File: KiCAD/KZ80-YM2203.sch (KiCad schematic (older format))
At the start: 32 parts, among them J1 SBC8080 BUS, J2 AD-JP1, J3 AD-JP1, J4 OUTPUT, U1 LM358, U2 74LS139, U3 74HCU04, U4 YM2203, U5 YM3014B, Y1 3.8MHz

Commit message: パス見直し
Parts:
- J1: symbol Z80-CPUB-rescue:Conn_02x20_Odd_Even -> KZ80-YM2203-rescue:Conn_02x20_Odd_Even-Z80-CPUB-rescue
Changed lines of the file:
@@
 EESchema Schematic File Version 4
+LIBS:KZ80-YM2203-cache
 EELAYER 30 0
 EELAYER END
@@
 	8300 1950 8350 1950
 $Comp
-L Z80-CPUB-rescue:Conn_02x20_Odd_Even J1
+L KZ80-YM2203-rescue:Conn_02x20_Odd_Even-Z80-CPUB-rescue J1
 U 1 1 5B55D8C4
 P 1150 1850
@@
 Wire Wire Line
 	2450 4600 2450 4700
+Connection ~ 2450 4600
+Wire Wire Line
+	2450 4600 2600 4600
 Wire Bus Line
 	1900 550  1900 3400
@@
 Wire Bus Line
 	600  550  600  4150
-Connection ~ 2450 4600
-Wire Wire Line
-	2450 4600 2600 4600
 $EndSCHEMATC

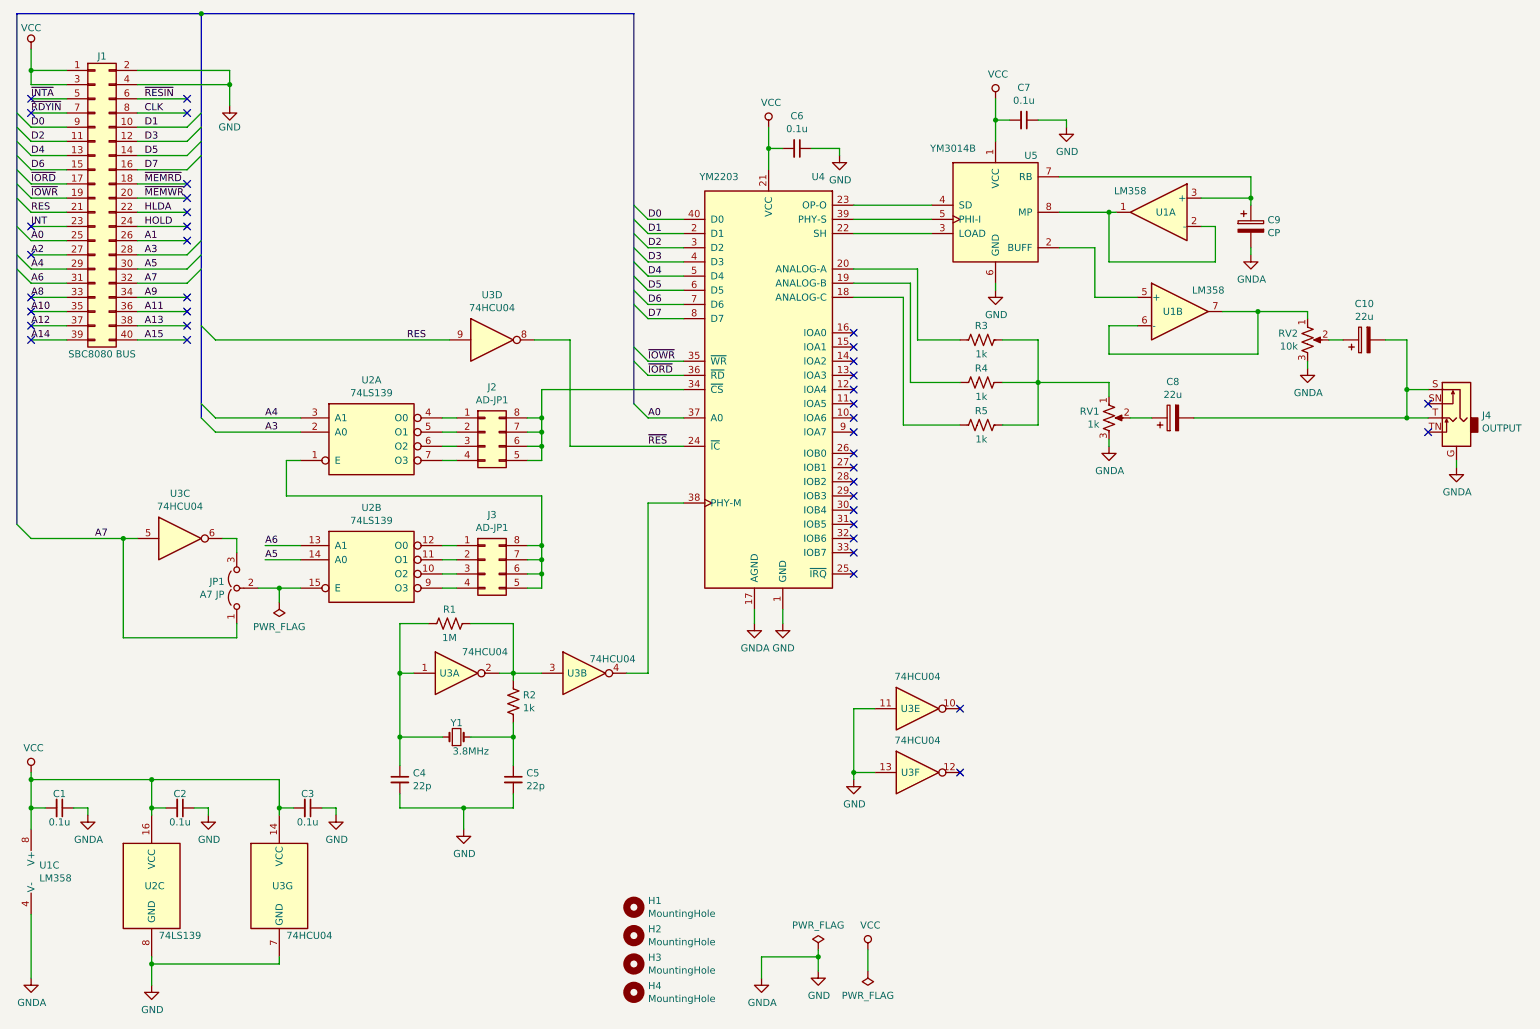
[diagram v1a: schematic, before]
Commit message: 回路図 間違いなど修正。出力段に抵抗器装着
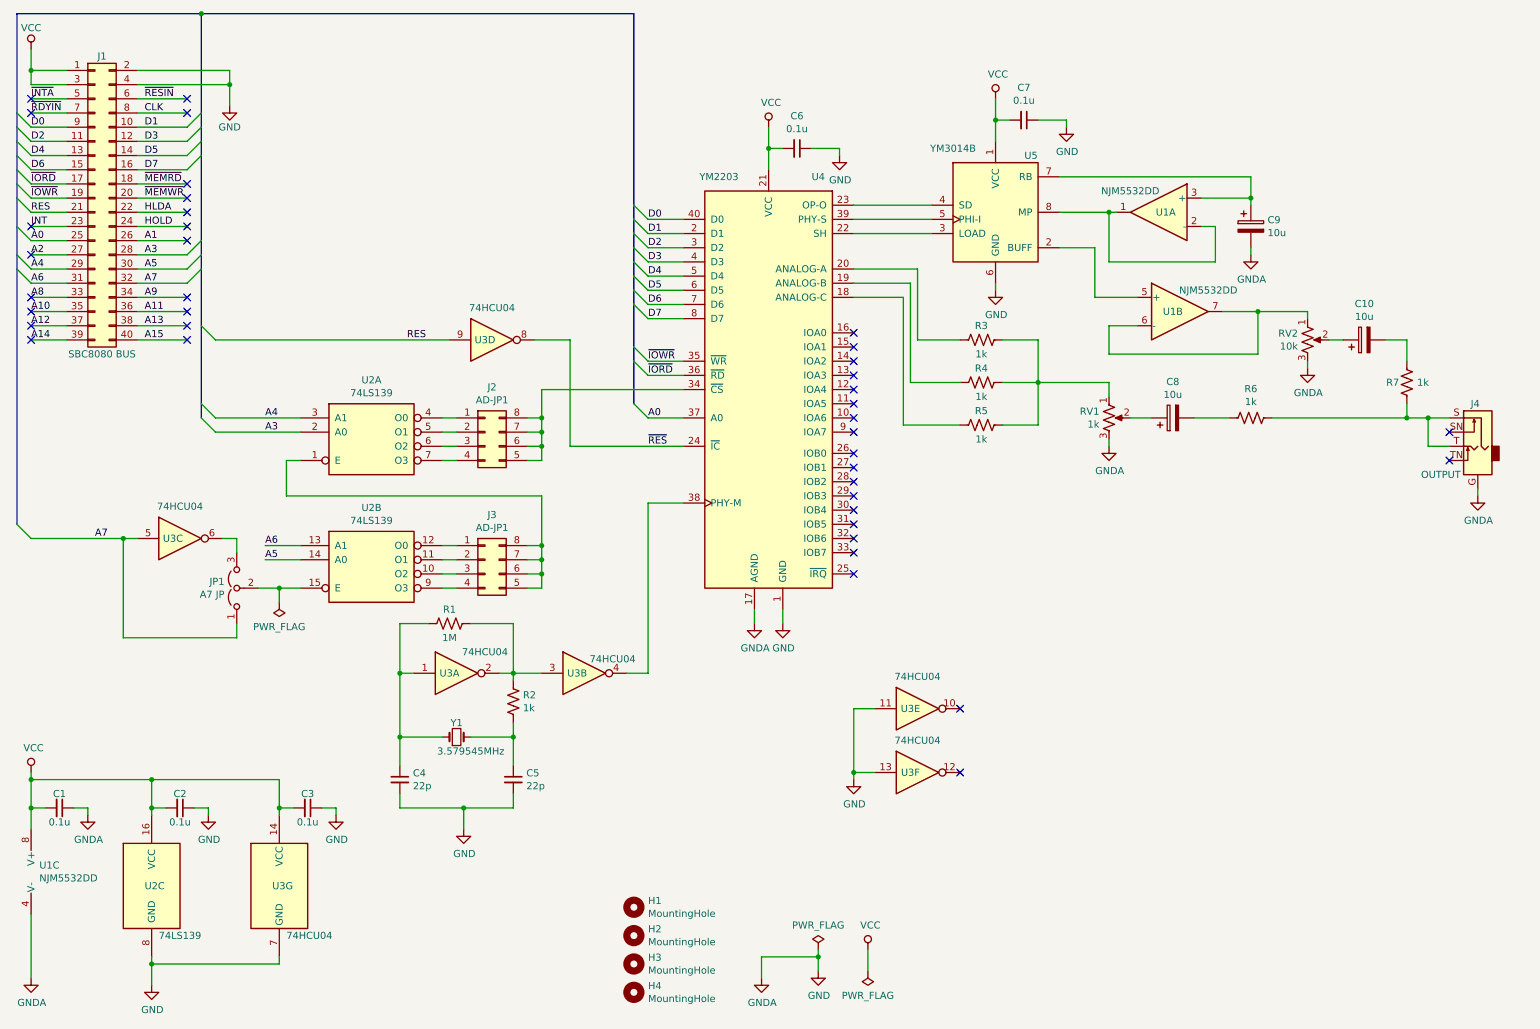
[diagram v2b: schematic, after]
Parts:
- added R6, R7: 1k, symbol Device:R_US
- C10, C8: value 22u -> 10u
- C9: value CP -> 10u
- U1: value LM358 -> NJM5532DD
- Y1: value 3.8MHz -> 3.579545MHz
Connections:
- net at J4.S, J4.T: now also R6.1, R7.1; no longer C10.2, C8.2
- new net: C8.2, R6.2
- new net: C10.2, R7.2
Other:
- moved on the sheet: J4
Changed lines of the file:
@@
 EESchema Schematic File Version 4
-LIBS:KZ80-YM2203-cache
 EELAYER 30 0
 EELAYER END
@@
 P 8650 1950
 F 0 "U1" H 8600 1950 50  0000 C CNN
-F 1 "LM358" H 8850 2100 50  0000 C CNN
+F 1 "NJM5532DD" H 8850 2100 50  0000 C CNN
 F 2 "" H 8650 1950 50  0001 C CNN
-F 3 "http://www.ti.com/lit/ds/symlink/lm2904-n.pdf" H 8650 1950 50  0001 C CNN
+F 3 "https://www.njr.co.jp/products/semicon/PDF/NJM5532_J.pdf" H 8650 1950 50  0001 C CNN
 	1    8650 1950
 	-1   0    0    -1
@@
 P 8800 2650
 F 0 "U1" H 8750 2650 50  0000 C CNN
-F 1 "LM358" H 9000 2800 50  0000 C CNN
+F 1 "NJM5532DD" H 9000 2800 50  0000 C CNN
 F 2 "" H 8800 2650 50  0001 C CNN
-F 3 "http://www.ti.com/lit/ds/symlink/lm2904-n.pdf" H 8800 2650 50  0001 C CNN
+F 3 "https://www.njr.co.jp/products/semicon/PDF/NJM5532_J.pdf" H 8800 2650 50  0001 C CNN
 	2    8800 2650
 	1    0    0    -1
@@
 P 800 6600
 F 0 "U1" H 758 6646 50  0000 L CNN
-F 1 "LM358" H 758 6555 50  0000 L CNN
+F 1 "NJM5532DD" H 758 6555 50  0000 L CNN
 F 2 "" H 800 6600 50  0001 C CNN
-F 3 "http://www.ti.com/lit/ds/symlink/lm2904-n.pdf" H 800 6600 50  0001 C CNN
+F 3 "https://www.njr.co.jp/products/semicon/PDF/NJM5532_J.pdf" H 800 6600 50  0001 C CNN
 	3    800  6600
 	1    0    0    -1
@@
 U 3 1 5FBD20EB
 P 1750 4250
-F 0 "U3" H 1750 4567 50  0000 C CNN
+F 0 "U3" H 1700 4250 50  0000 C CNN
 F 1 "74HCU04" H 1750 4476 50  0000 C CNN
 F 2 "" H 1750 4250 50  0001 C CNN
@@
 U 4 1 5FBD28D0
 P 3950 2850
-F 0 "U3" H 3950 3167 50  0000 C CNN
+F 0 "U3" H 3900 2850 50  0000 C CNN
 F 1 "74HCU04" H 3950 3076 50  0000 C CNN
 F 2 "" H 3950 2850 50  0001 C CNN
@@
 P 3700 5650
 F 0 "Y1" H 3700 5750 50  0000 C CNN
-F 1 "3.8MHz" H 3800 5550 50  0000 C CNN
+F 1 "3.579545MHz" H 3800 5550 50  0000 C CNN
 F 2 "" H 3700 5650 50  0001 C CNN
 F 3 "~" H 3700 5650 50  0001 C CNN
@@
 P 8750 3400
 F 0 "C8" V 9005 3400 50  0000 C CNN
-F 1 "22u" V 8914 3400 50  0000 C CNN
+F 1 "10u" V 8914 3400 50  0000 C CNN
 F 2 "" H 8788 3250 50  0001 C CNN
 F 3 "~" H 8750 3400 50  0001 C CNN
@@
 P 10100 2850
 F 0 "C10" V 10355 2850 50  0000 C CNN
-F 1 "22u" V 10264 2850 50  0000 C CNN
+F 1 "10u" V 10264 2850 50  0000 C CNN
 F 2 "" H 10138 2700 50  0001 C CNN
 F 3 "~" H 10100 2850 50  0001 C CNN
@@
 Wire Wire Line
 	8450 3400 8600 3400
-Wire Wire Line
-	8900 3400 10400 3400
-Wire Wire Line
-	10400 3400 10400 3200
 Wire Wire Line
 	10400 2850 10250 2850
@@
 L Connector:AudioJack2_Ground_Switch J4
 U 1 1 60090806
-P 10750 3400
-F 0 "J4" H 10570 3418 50  0000 R CNN
-F 1 "OUTPUT" H 10570 3327 50  0000 R CNN
-F 2 "" H 10750 3600 50  0001 C CNN
-F 3 "~" H 10750 3600 50  0001 C CNN
-	1    10750 3400
+P 10900 3600
+F 0 "J4" H 10950 3900 50  0000 R CNN
+F 1 "OUTPUT" H 11300 3400 50  0000 R CNN
+F 2 "" H 10900 3800 50  0001 C CNN
+F 3 "~" H 10900 3800 50  0001 C CNN
+	1    10900 3600
 	-1   0    0    -1
 $EndComp
-Wire Wire Line
-	10400 3400 10550 3400
-Connection ~ 10400 3400
-Wire Wire Line
-	10400 3200 10550 3200
-Connection ~ 10400 3200
-Wire Wire Line
-	10400 3200 10400 2850
-NoConn ~ 10550 3300
-NoConn ~ 10550 3500
-$Comp
-L power:GNDA #PWR024
-U 1 1 600D75A0
-P 10750 3750
-F 0 "#PWR024" H 10750 3500 50  0001 C CNN
-F 1 "GNDA" H 10755 3577 50  0000 C CNN
-F 2 "" H 10750 3750 50  0001 C CNN
-F 3 "" H 10750 3750 50  0001 C CNN
-	1    10750 3750
-	1    0    0    -1
-$EndComp
-Wire Wire Line
-	10750 3700 10750 3750
+NoConn ~ 10700 3500
+NoConn ~ 10700 3700
 $Comp
 L Device:CP C9
@@
 P 9300 2050
 F 0 "C9" H 9418 2096 50  0000 L CNN
-F 1 "CP" H 9418 2005 50  0000 L CNN
+F 1 "10u" H 9418 2005 50  0000 L CNN
 F 2 "" H 9338 1900 50  0001 C CNN
 F 3 "~" H 9300 2050 50  0001 C CNN
@@
 Wire Wire Line
 	2450 4600 2600 4600
-Wire Bus Line
-	1900 550  1900 3400
+Wire Wire Line
+	10900 3900 10900 3950
+$Comp
+L power:GNDA #PWR024
+U 1 1 600D75A0
+P 10900 3950
+F 0 "#PWR024" H 10900 3700 50  0001 C CNN
+F 1 "GNDA" H 10905 3777 50  0000 C CNN
+F 2 "" H 10900 3950 50  0001 C CNN
+F 3 "" H 10900 3950 50  0001 C CNN
+	1    10900 3950
+	1    0    0    -1
+$EndComp
+$Comp
+L Device:R_US R6
+U 1 1 5FCD251E
+P 9300 3400
+F 0 "R6" V 9095 3400 50  0000 C CNN
+F 1 "1k" V 9186 3400 50  0000 C CNN
+F 2 "" V 9340 3390 50  0001 C CNN
+F 3 "~" H 9300 3400 50  0001 C CNN
+	1    9300 3400
+	0    1    1    0
+$EndComp
+$Comp
+L Device:R_US R7
+U 1 1 5FD00CC1
+P 10400 3150
+F 0 "R7" H 10500 3150 50  0000 C CNN
+F 1 "1k" H 10286 3150 50  0000 C CNN
+F 2 "" V 10440 3140 50  0001 C CNN
+F 3 "~" H 10400 3150 50  0001 C CNN
+	1    10400 3150
+	-1   0    0    1
+$EndComp
+Wire Wire Line
+	10400 2850 10400 3000
+Wire Wire Line
+	8900 3400 9150 3400
+Wire Wire Line
+	9450 3400 10400 3400
+Wire Wire Line
+	10400 3300 10400 3400
+Connection ~ 10400 3400
+Wire Wire Line
+	10400 3400 10550 3400
+Wire Wire Line
+	10550 3400 10550 3600
+Wire Wire Line
+	10550 3600 10700 3600
 Wire Bus Line
 	4950 550  4950 3300
 Wire Bus Line
 	600  550  600  4150
+Wire Bus Line
+	1900 550  1900 3400
+Connection ~ 10550 3400
+Wire Wire Line
+	10550 3400 10700 3400
 $EndSCHEMATC

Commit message: 基板パターン検討・ガーバーデータ出力
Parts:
- removed J4: OUTPUT, symbol Connector:AudioJack2_Ground_Switch
- added C11: 10u, Capacitor_THT:CP_Radial_D5.0mm_P2.50mm, symbol Device:CP
- added J4: Audio-Jack, AJ-1780:AJ-1780, symbol AJ-1780:Audio-Jack-3_2Switches-YM2151-rescue
- added J5: A-CON, Connector_PinHeader_2.54mm:PinHeader_2x07_P2.54mm_Vertical, symbol Connector_Generic:Conn_02x07_Odd_Even
- added J6: B-CON, Connector_PinHeader_2.54mm:PinHeader_2x07_P2.54mm_Vertical, symbol Connector_Generic:Conn_02x07_Odd_Even
- added NT1: Net-Tie_2, NetTie:NetTie-2_SMD_Pad2.0mm, symbol Device:Net-Tie_2
- C1, C2, C3, C4, C5, C6, C7: footprint (none) -> Capacitor_THT:C_Disc_D3.0mm_W1.6mm_P2.50mm
- C10, C8, C9: footprint (none) -> Capacitor_THT:CP_Radial_D5.0mm_P2.50mm
- H1, H2, H3, H4: footprint (none) -> MountingHole:MountingHole_3.2mm_M3
- J2, J3: footprint (none) -> Connector_PinHeader_2.54mm:PinHeader_2x04_P2.54mm_Vertical; symbol Connector_Generic:Conn_02x04_Counter_Clockwise -> Connector_Generic:Conn_02x04_Odd_Even
- JP1: footprint (none) -> Connector_PinHeader_2.54mm:PinHeader_1x03_P2.54mm_Vertical
- R1, R2, R3, R4, R5, R6, R7: footprint (none) -> Resistor_THT:R_Axial_DIN0207_L6.3mm_D2.5mm_P10.16mm_Horizontal
- RV1, RV2: footprint (none) -> Potentiometer_THT:Potentiometer_Vishay_T73YP_Vertical
- U1: footprint (none) -> Package_DIP:DIP-8_W7.62mm_Socket
- U2: value 74LS139 -> 74HC139; footprint (none) -> Package_DIP:DIP-16_W7.62mm_Socket
- U3: footprint (none) -> Package_DIP:DIP-14_W7.62mm_Socket
- U4: footprint (none) -> Package_DIP:DIP-40_W15.24mm_Socket
- U5: footprint (none) -> Package_DIP:DIP-8_W7.62mm
- Y1: footprint (none) -> Crystal:Crystal_HC49-U_Vertical
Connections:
- net GND: now also C11.1, J5.14 (Pin_14), J6.14 (Pin_14), NT1.2; no longer C1.1, C7.1, C9.2, RV1.3, RV2.3, U1.4 (V-), U5.6 (GND)
- net VCC: now also C11.2, J5.13 (Pin_13), J6.13 (Pin_13)
- net IOA6: now reaches U4.10 (IOA6)
- net IOA6: now also J5.7 (Pin_7)
- net IOA5: now reaches U4.11 (IOA5)
- net IOA5: now also J5.6 (Pin_6)
- net IOA4: now reaches U4.12 (IOA4)
- net IOA4: now also J5.5 (Pin_5)
- net IOA3: now reaches U4.13 (IOA3)
- net IOA3: now also J5.4 (Pin_4)
- net IOA2: now reaches U4.14 (IOA2)
- net IOA2: now also J5.3 (Pin_3)
- net IOA1: now reaches U4.15 (IOA1)
- net IOA1: now also J5.2 (Pin_2)
- net IOA0: now reaches U4.16 (IOA0)
- net IOA0: now also J5.1 (Pin_1)
- net ~IRQ: now reaches U4.25 (~IRQ)
- net ~IRQ: now also J5.12 (Pin_12), J6.12 (Pin_12)
- net IOB0: now reaches U4.26 (IOB0)
- net IOB0: now also J6.1 (Pin_1)
- net IOB1: now reaches U4.27 (IOB1)
- net IOB1: now also J6.2 (Pin_2)
- net IOB2: now reaches U4.28 (IOB2)
- net IOB2: now also J6.3 (Pin_3)
- net IOB3: now reaches U4.29 (IOB3)
- net IOB3: now also J6.4 (Pin_4)
- net IOB4: now reaches U4.30 (IOB4)
- net IOB4: now also J6.5 (Pin_5)
- net IOB5: now reaches U4.31 (IOB5)
- net IOB5: now also J6.6 (Pin_6)
- net IOB6: now reaches U4.32 (IOB6)
- net IOB6: now also J6.7 (Pin_7)
- net IOB7: now reaches U4.33 (IOB7)
- net IOB7: now also J6.8 (Pin_8)
- net at J2.6 (Pin_6), J2.8 (Pin_8), U4.34 (~CS): now also J2.2 (Pin_2), J2.4 (Pin_4); no longer J2.5 (Pin_5), J2.7 (Pin_7)
- net IOA7: now reaches U4.9 (IOA7)
- net IOA7: now also J5.8 (Pin_8)
- net at J3.6 (Pin_6), J3.8 (Pin_8), U2.1 (E): now also J3.2 (Pin_2), J3.4 (Pin_4); no longer J3.5 (Pin_5), J3.7 (Pin_7)
- net at U2.5 (O1): now also J2.3 (Pin_3); no longer J2.2 (Pin_2)
- net at U2.6 (O2): now also J2.5 (Pin_5); no longer J2.3 (Pin_3)
- net at U2.7 (O3): now also J2.7 (Pin_7); no longer J2.4 (Pin_4)
- net at U2.10 (O2): now also J3.5 (Pin_5); no longer J3.3 (Pin_3)
- net at U2.11 (O1): now also J3.3 (Pin_3); no longer J3.2 (Pin_2)
- net at U2.9 (O3): now also J3.7 (Pin_7); no longer J3.4 (Pin_4)
- net at R6.1, R7.1: now also J4.2, J4.5
- new net GNDA: C1.1, C7.1, C9.2, J4.1, NT1.1, RV1.3, RV2.3, U1.4 (V-), U5.6 (GND)
- no-connect marks 40 -> 29
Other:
- moved on the sheet: H1, H2, H3, H4, U3E, U3F
